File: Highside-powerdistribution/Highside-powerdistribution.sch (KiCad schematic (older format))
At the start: 43 parts, among them J1 Conn_01x02_Male, J10 Screw_Terminal_01x02, J11 Screw_Terminal_01x02, J12 Screw_Terminal_01x02, J13 Screw_Terminal_01x02, J14 Conn_01x02, J15 Screw_Terminal_01x06, J2 Conn_01x02_Male, J3 Conn_01x02_Male, J4 Conn_01x02_Male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

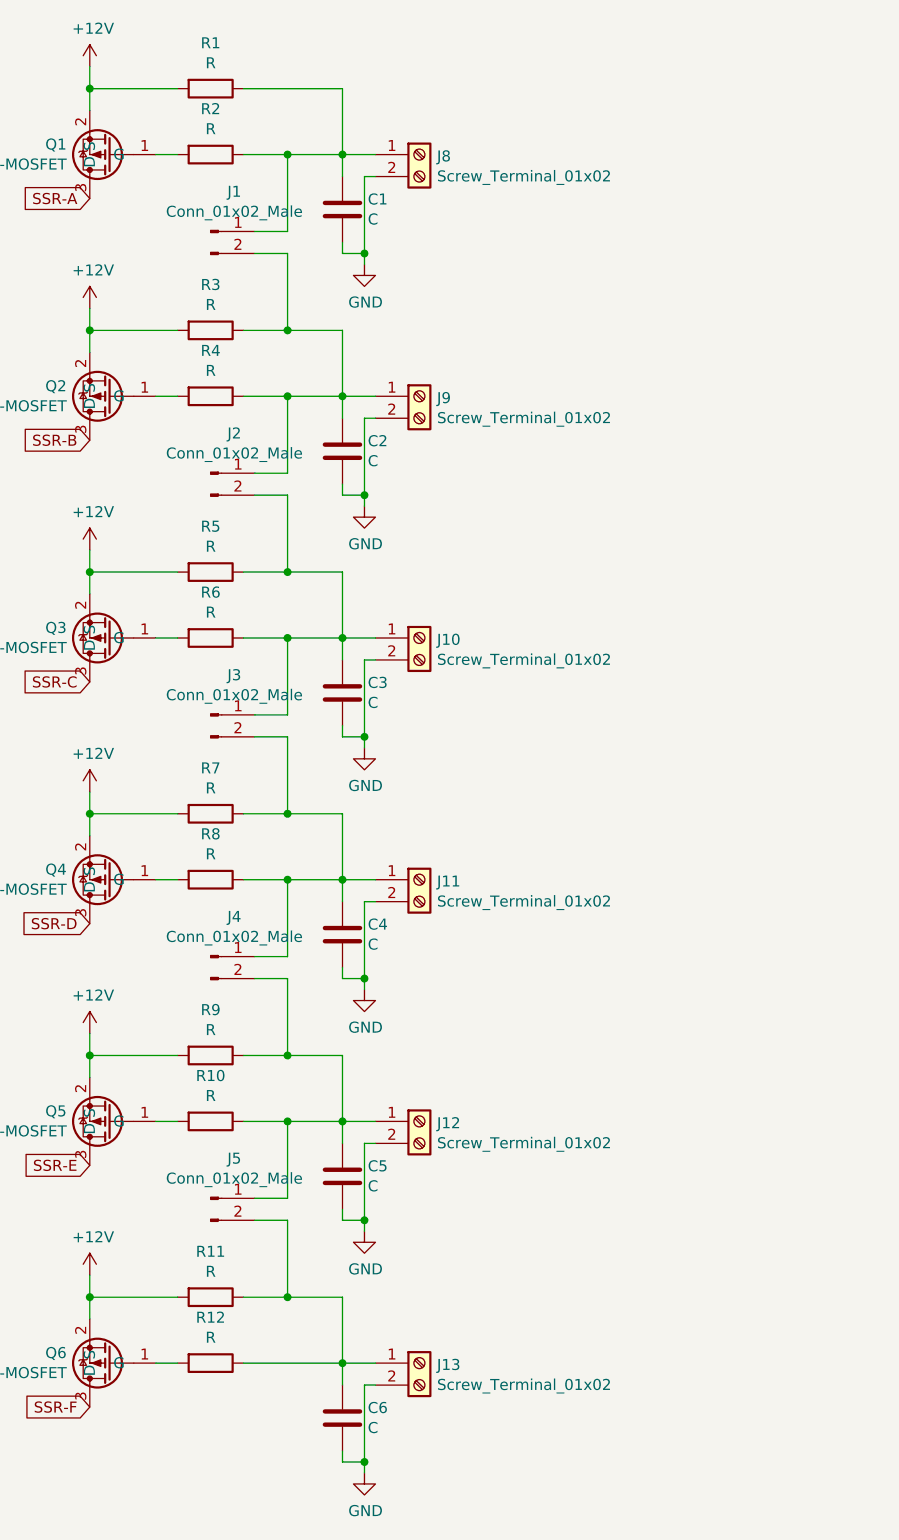
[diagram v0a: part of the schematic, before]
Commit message: Changed fuses and added more 3D files.
Changed to ATO fuses
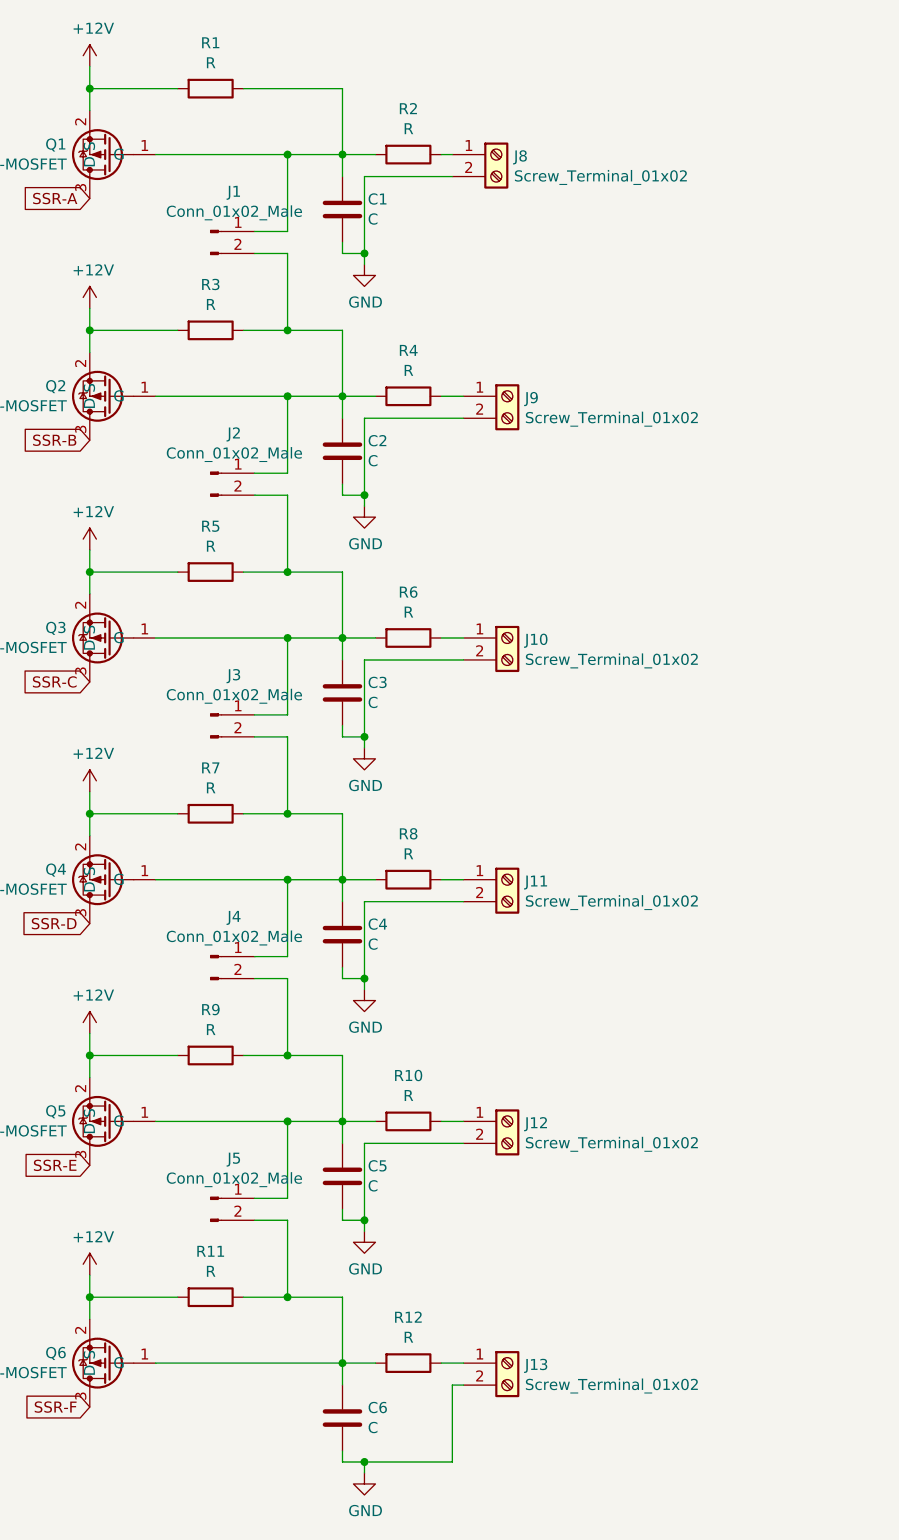
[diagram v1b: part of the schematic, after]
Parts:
- F1, F2, F3, F4, F5, F6: footprint Highside-powerdistribution:PTF-15 -> Highside-powerdistribution:ATO_Fuseholder_3522-2
- J10, J11, J12, J13, J8, J9: footprint Highside-powerdistribution:PTSA 1,5 2-3,5-Z -> Highside-powerdistribution:PTSA1,5-2-3,5-Z
- J15: footprint Highside-powerdistribution:ETB11060B000Z -> Highside-powerdistribution:20.101M-6
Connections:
- net at Q1.1 (G), R2.2: now also C1.1, J1.1 (Pin_1), R1.1
- net at Q2.1 (G), R4.2: now also C2.1, J1.2 (Pin_2), J2.1 (Pin_1), R3.1
- net at Q3.1 (G), R6.2: now also C3.1, J2.2 (Pin_2), J3.1 (Pin_1), R5.1
- net at Q4.1 (G), R8.2: now also C4.1, J3.2 (Pin_2), J4.1 (Pin_1), R7.1
- net at Q5.1 (G), R10.2: now also C5.1, J4.2 (Pin_2), J5.1 (Pin_1), R9.1
- net at C6.1, J5.2 (Pin_2), R11.1: now also Q6.1 (G), R12.2; no longer J13.1 (Pin_1), R12.1
- new net: J8.1 (Pin_1), R2.1
- new net: J13.1 (Pin_1), R12.1
- new net: J9.1 (Pin_1), R4.1
- new net: J10.1 (Pin_1), R6.1
- new net: J11.1 (Pin_1), R8.1
- new net: J12.1 (Pin_1), R10.1
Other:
- moved on the sheet: J10, J11, J12, J13, J8, J9, R10, R12, R2, R4, R6, R8
